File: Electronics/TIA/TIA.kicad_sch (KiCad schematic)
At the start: 4 parts

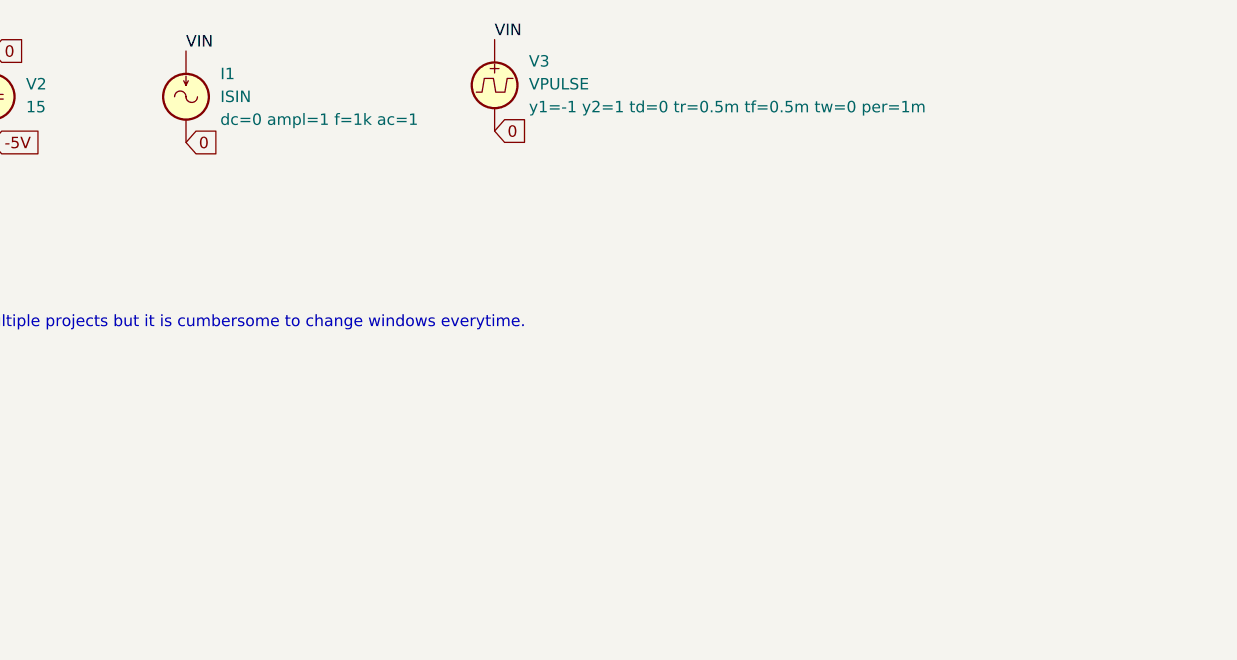
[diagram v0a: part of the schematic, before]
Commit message: Make the simulation circuit tidier
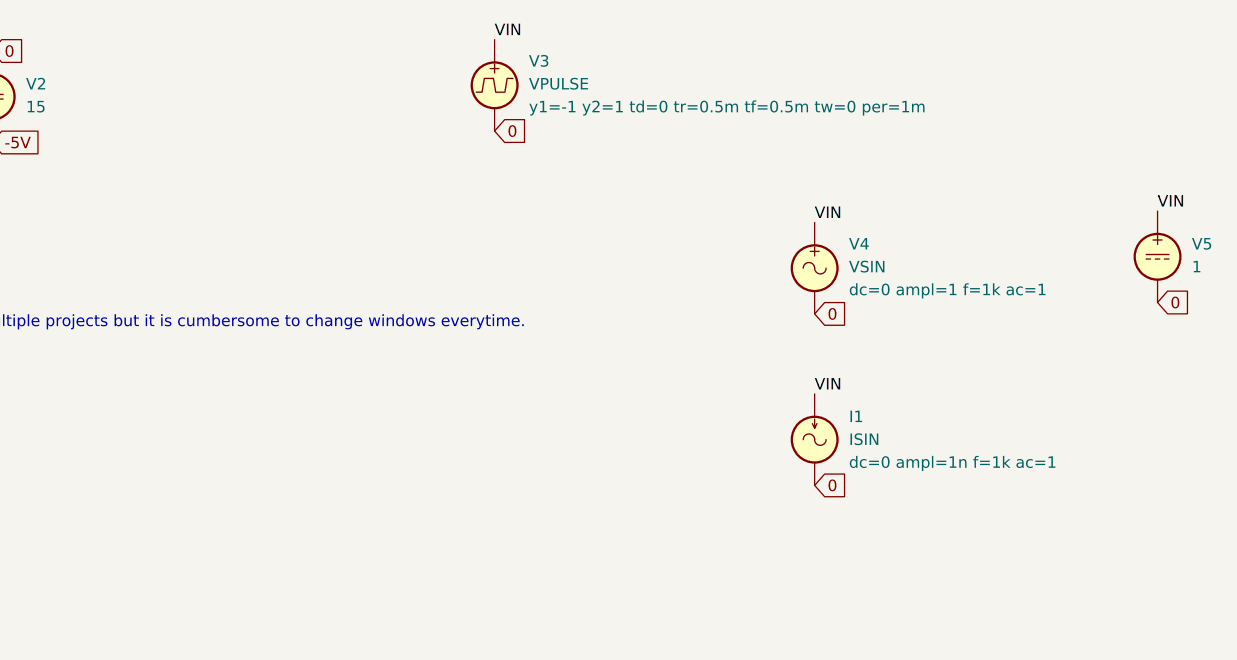
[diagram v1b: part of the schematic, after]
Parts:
- added V4: VSIN, symbol Simulation_SPICE:VSIN
- added V5: 1, symbol Simulation_SPICE:VDC
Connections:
- net 0: now also V4.2, V5.2
- net VIN: now also V4.1, V5.1
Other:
- moved on the sheet: I1
